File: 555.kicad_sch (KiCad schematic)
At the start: 62 parts, among them J2 Screw_Terminal_01x02, P1 USB_C_Plug, SW1 SW_Push, SW2 SW_Push, SW3 SW_Push, SW4 SW_Push, SW5 SW_Push, SW6 SW_Push, SW7 SW_Push, SW8 SW_Push, U1 NE555P

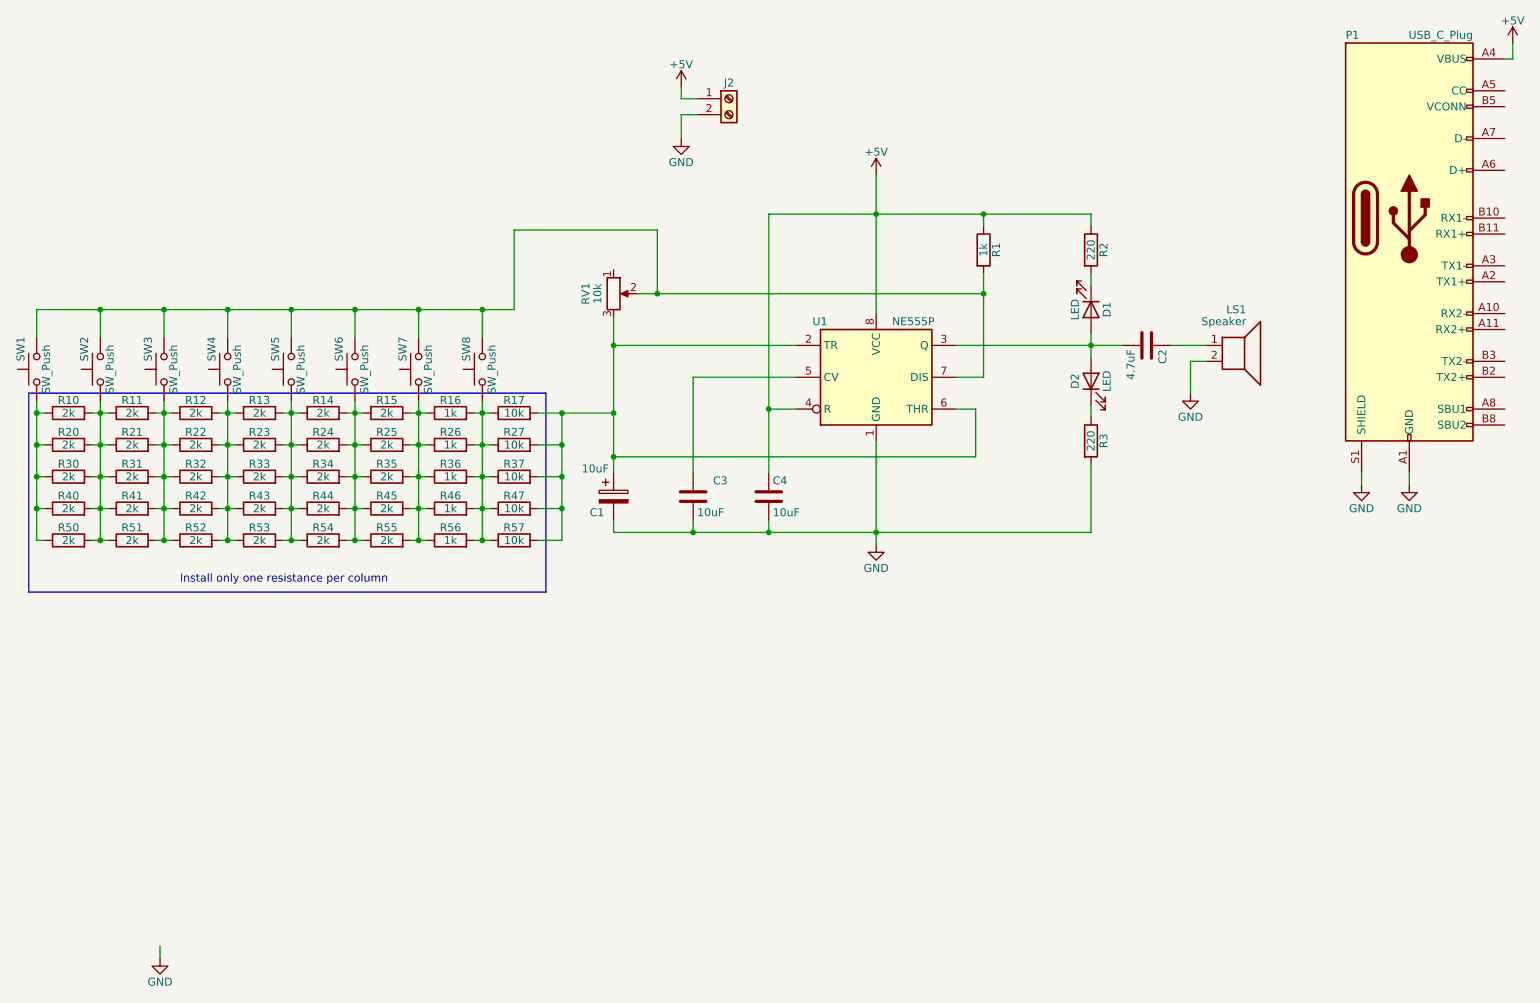
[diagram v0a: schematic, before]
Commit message: Simpler, remove the 10k resistor, move the potentiometer to full to play
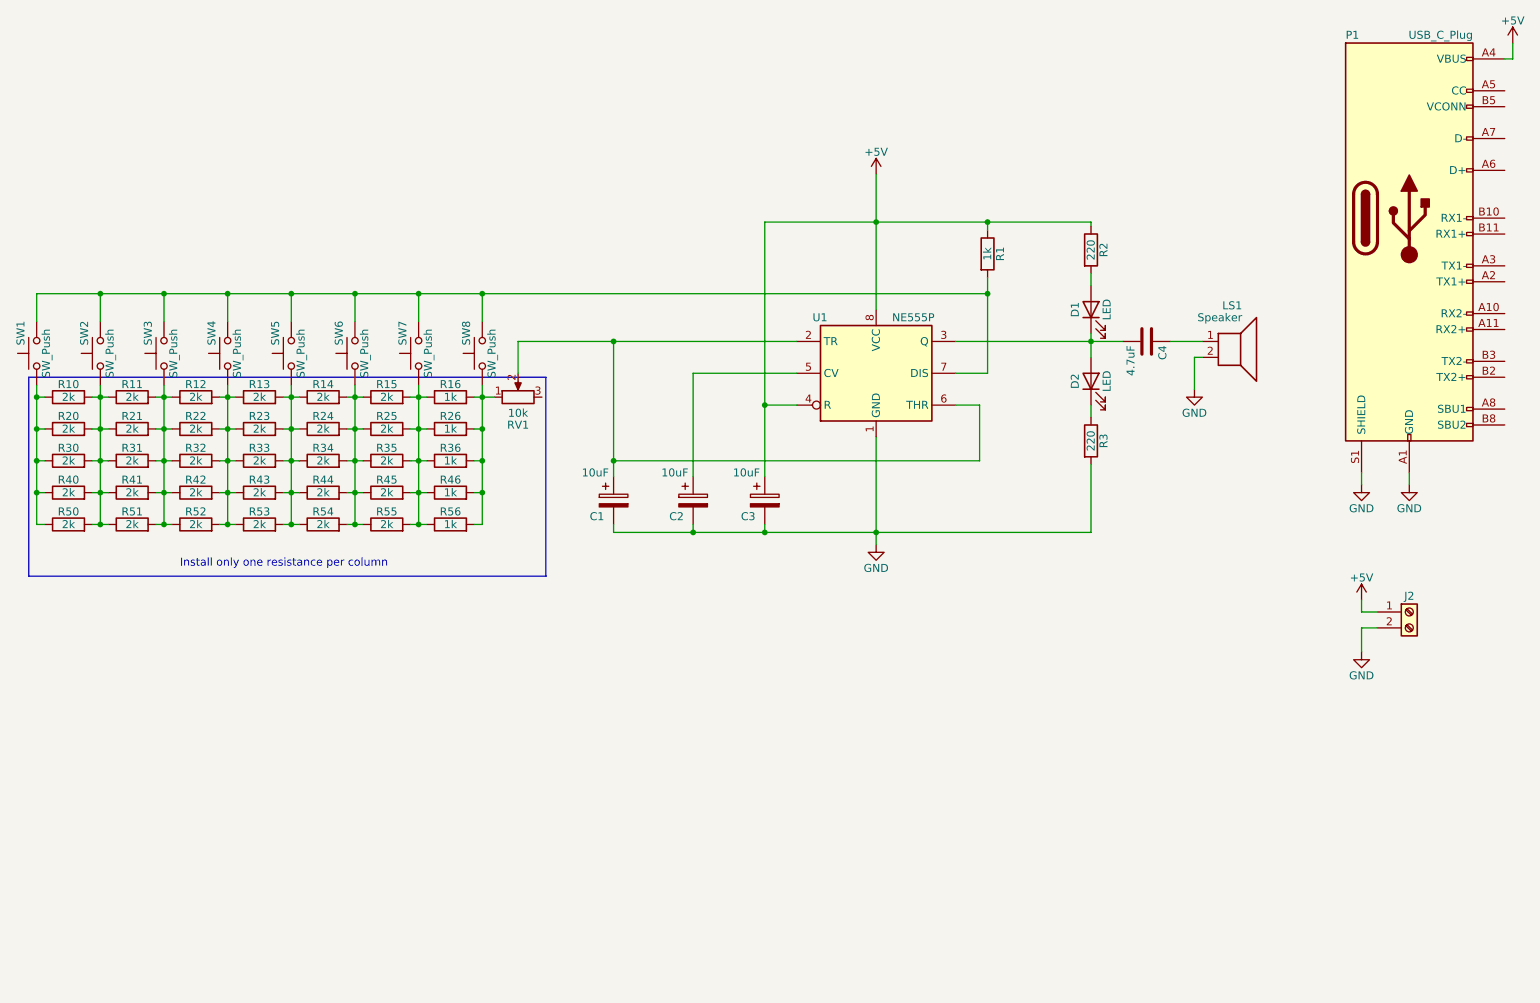
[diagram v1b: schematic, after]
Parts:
- removed C3, C4: 10uF, Capacitor_THT:CP_Radial_D5.0mm_P2.00mm, symbol Device:C
- removed R17: 10k, Resistor_THT:R_Axial_DIN0207_L6.3mm_D2.5mm_P10.16mm_Horizontal, symbol Device:R
- removed R27: 10k, Resistor_SMD:R_1206_3216Metric, symbol Device:R
- removed R37: 10k, Resistor_SMD:R_0603_1608Metric, symbol Device:R
- removed R47: 10k, Resistor_SMD:R_0402_1005Metric, symbol Device:R
- removed R57: 10k, Resistor_SMD:R_0201_0603Metric, symbol Device:R
- added C2, C3: 10uF, Capacitor_THT:CP_Radial_D5.0mm_P2.00mm, symbol Device:C_Polarized
- renumbered C2 to C4
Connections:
- net +5V: now also C3.1
- net GND: now also C2.2, C3.2
- net at R16.2, R26.2, R36.2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: now also RV1.1
- net at C1.1, U1.2 (TR), U1.6 (THR): now also RV1.2; no longer RV1.3
- net at U1.5 (CV): now also C2.1
- net at R2.2: now also D1.2 (A); no longer D1.1 (K)
- net at R1.2, SW1.2, SW2.2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: no longer RV1.2
- net at C4.2, D2.2 (A), U1.3 (Q): now also D1.1 (K); no longer D1.2 (A)
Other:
- moved on the sheet: C1, C4, D1, J2, LS1, R1, R10, R11, R12, R13, R14, R15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

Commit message: PCB updated
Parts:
- removed C4: 4.7uF, Capacitor_THT:CP_Radial_D5.0mm_P2.00mm, symbol Device:C
- added C4: 10uF, Capacitor_THT:CP_Radial_D5.0mm_P2.00mm, symbol Device:C_Polarized
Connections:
- net at D1.1 (K), D2.2 (A), U1.3 (Q): now also C4.1
- net at LS1.1: now also C4.2
- no-connect marks 0 -> 14
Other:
- moved on the sheet: P1
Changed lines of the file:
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@@
   (junction (at 75.565 116.84) (diameter 0) (color 0 0 0 0)
   )
+  (no_connect (at 279.4 99.06))
+  (no_connect (at 279.4 60.96))
+  (no_connect (at 279.4 96.52))
+  (no_connect (at 279.4 55.88))
+  (no_connect (at 279.4 81.28))
+  (no_connect (at 279.4 73.66))
+  (no_connect (at 279.4 66.04))
+  (no_connect (at 279.4 88.9))
+  (no_connect (at 279.4 83.82))
+  (no_connect (at 279.4 106.68))
+  (no_connect (at 279.4 91.44))
+  (no_connect (at 279.4 53.34))
+  (no_connect (at 279.4 104.14))
+  (no_connect (at 279.4 76.2))
   (wire (pts (xy 53.975 111.76) (xy 55.245 111.76))
     (stroke (width 0) (type default) (color 0 0 0 0))
@@
     (stroke (width 0) (type default) (color 0 0 0 0))
   )
-  (wire (pts (xy 264.16 113.665) (xy 264.16 115.57))
+  (wire (pts (xy 264.16 114.3) (xy 264.16 115.57))
     (stroke (width 0) (type default) (color 0 0 0 0))
   )
@@
     (stroke (width 0) (type default) (color 0 0 0 0))
   )
-  (wire (pts (xy 280.67 47.625) (xy 280.67 45.085))
+  (wire (pts (xy 280.67 48.26) (xy 280.67 45.72))
     (stroke (width 0) (type default) (color 0 0 0 0))
   )
@@
     (stroke (width 0) (type default) (color 0 0 0 0))
   )
-  (wire (pts (xy 279.4 47.625) (xy 280.67 47.625))
+  (wire (pts (xy 279.4 48.26) (xy 280.67 48.26))
     (stroke (width 0) (type default) (color 0 0 0 0))
   )
@@
     (stroke (width 0) (type default) (color 0 0 0 0))
   )
-  (wire (pts (xy 256.54 113.665) (xy 256.54 115.57))
+  (wire (pts (xy 256.54 114.3) (xy 256.54 115.57))
     (stroke (width 0) (type default) (color 0 0 0 0))
   )
@@
     (pin "2")
   )
-  (symbol (lib_id "power:+5V") (at 280.67 45.085 0) (unit 1)
-    (in_bom yes) (on_board yes)
-    (property "Reference" "#PWR0108" (id 0) (at 280.67 48.895 0)
-      (effects (font (size 1.27 1.27)) hide)
-    )
-    (property "Value" "+5V" (id 1) (at 280.67 41.529 0))
-    (property "Footprint" "" (id 2) (at 280.67 45.085 0)
-      (effects (font (size 1.27 1.27)) hide)
-    )
-    (property "Datasheet" "" (id 3) (at 280.67 45.085 0)
+  (symbol (lib_id "power:+5V") (at 280.67 45.72 0) (unit 1)
+    (in_bom yes) (on_board yes)
+    (property "Reference" "#PWR0108" (id 0) (at 280.67 49.53 0)
+      (effects (font (size 1.27 1.27)) hide)
+    )
+    (property "Value" "+5V" (id 1) (at 280.67 42.164 0))
+    (property "Footprint" "" (id 2) (at 280.67 45.72 0)
+      (effects (font (size 1.27 1.27)) hide)
+    )
+    (property "Datasheet" "" (id 3) (at 280.67 45.72 0)
       (effects (font (size 1.27 1.27)) hide)
     )
@@
     )
     (property "Vendor" "Digikey" (id 5) (at 111.125 111.76 0)
+      (effects (font (size 1.27 1.27)) hide)
+    )
+    (pin "1")
+    (pin "2")
+  )
+  (symbol (lib_id "Device:C_Polarized") (at 222.25 92.71 90) (unit 1)
+    (in_bom yes) (on_board yes)
+    (property "Reference" "C4" (id 0) (at 224.79 96.52 0)
+      (effects (font (size 1.27 1.27)) (justify left))
+    )
+    (property "Value" "10uF" (id 1) (at 217.805 97.79 0)
+      (effects (font (size 1.27 1.27)) (justify left))
+    )
+    (property "Footprint" "Capacitor_THT:CP_Radial_D5.0mm_P2.00mm" (id 2) (at 226.06 91.7448 0)
+      (effects (font (size 1.27 1.27)) hide)
+    )
+    (property "Datasheet" "~" (id 3) (at 222.25 92.71 0)
+      (effects (font (size 1.27 1.27)) hide)
+    )
+    (property "Manufacturer part number" "732-8625-1-ND" (id 4) (at 222.25 92.71 0)
+      (effects (font (size 1.27 1.27)) hide)
+    )
+    (property "Vendor" "Digikey" (id 5) (at 222.25 92.71 0)
       (effects (font (size 1.27 1.27)) hide)
     )
@@
     (pin "7")
   )
-  (symbol (lib_id "Connector:USB_C_Plug") (at 264.16 73.025 0) (unit 1)
-    (in_bom yes) (on_board yes)
-    (property "Reference" "P1" (id 0) (at 254 43.815 0)
+  (symbol (lib_id "Connector:USB_C_Plug") (at 264.16 73.66 0) (unit 1)
+    (in_bom yes) (on_board yes)
+    (property "Reference" "P1" (id 0) (at 254 44.45 0)
       (effects (font (size 1.27 1.27)) (justify left))
     )
-    (property "Value" "USB_C_Plug" (id 1) (at 274.32 43.815 0)
+    (property "Value" "USB_C_Plug" (id 1) (at 274.32 44.45 0)
       (effects (font (size 1.27 1.27)) (justify right))
     )
-    (property "Footprint" "Connector_USB:USB_C_Receptacle_GCT_USB4085" (id 2) (at 267.97 73.025 0)
-      (effects (font (size 1.27 1.27)) hide)
-    )
-    (property "Datasheet" "https://www.usb.org/sites/default/files/documents/usb_type-c.zip" (id 3) (at 267.97 73.025 0)
-      (effects (font (size 1.27 1.27)) hide)
-    )
-    (property "Manufacturer part number" "2073-USB4085-GF-ACT-ND" (id 4) (at 264.16 73.025 0)
-      (effects (font (size 1.27 1.27)) hide)
-    )
-    (property "Vendor" "Digikey" (id 5) (at 264.16 73.025 0)
+    (property "Footprint" "Connector_USB:USB_C_Receptacle_GCT_USB4085" (id 2) (at 267.97 73.66 0)
+      (effects (font (size 1.27 1.27)) hide)
+    )
+    (property "Datasheet" "https://www.usb.org/sites/default/files/documents/usb_type-c.zip" (id 3) (at 267.97 73.66 0)
+      (effects (font (size 1.27 1.27)) hide)
+    )
+    (property "Manufacturer part number" "2073-USB4085-GF-ACT-ND" (id 4) (at 264.16 73.66 0)
+      (effects (font (size 1.27 1.27)) hide)
+    )
+    (property "Vendor" "Digikey" (id 5) (at 264.16 73.66 0)
       (effects (font (size 1.27 1.27)) hide)
     )
@@
     (pin "2")
   )
-  (symbol (lib_id "Device:C") (at 222.25 92.71 270) (unit 1)
-    (in_bom yes) (on_board yes)
-    (property "Reference" "C4" (id 0) (at 224.79 93.345 0)
-      (effects (font (size 1.27 1.27)) (justify left))
-    )
-    (property "Value" "4.7uF" (id 1) (at 219.71 93.345 0)
-      (effects (font (size 1.27 1.27)) (justify left))
-    )
-    (property "Footprint" "Capacitor_THT:CP_Radial_D5.0mm_P2.00mm" (id 2) (at 218.44 93.6752 0)
-      (effects (font (size 1.27 1.27)) hide)
-    )
-    (property "Datasheet" "~" (id 3) (at 222.25 92.71 0)
-      (effects (font (size 1.27 1.27)) hide)
-    )
-    (property "Manufacturer part number" "732-8624-1-ND" (id 4) (at 222.25 92.71 0)
-      (effects (font (size 1.27 1.27)) hide)
-    )
-    (property "Vendor" "Digikey" (id 5) (at 222.25 92.71 0)
-      (effects (font (size 1.27 1.27)) hide)
-    )
-    (pin "1")
-    (pin "2")
-  )
   (symbol (lib_id "Device:R_Potentiometer") (at 121.92 101.6 90) (unit 1)
     (in_bom yes) (on_board yes)
@@
       (reference "C3") (unit 1) (value "10uF") (footprint "Capacitor_THT:CP_Radial_D5.0mm_P2.00mm")
     )
-    (path "/eb43cd7a-b92d-4126-827e-05ce5f51b08c"
-      (reference "C4") (unit 1) (value "4.7uF") (footprint "Capacitor_THT:CP_Radial_D5.0mm_P2.00mm")
+    (path "/82891a1c-a18b-4efc-9f51-de6998f62d8c"
+      (reference "C4") (unit 1) (value "10uF") (footprint "Capacitor_THT:CP_Radial_D5.0mm_P2.00mm")
     )
     (path "/9f5756e1-f166-4e69-8e27-f4d7349d5b5c"

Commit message: Prettier sch
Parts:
- removed P1: USB_C_Plug, Connector_USB:USB_C_Receptacle_GCT_USB4085, symbol Connector:USB_C_Plug
- added P1: USB_C_Plug_USB2.0, Connector_USB:USB_C_Receptacle_GCT_USB4085, symbol Connector:USB_C_Plug_USB2.0
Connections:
- net +5V: now also P1.A4 (VBUS), P1.A9 (VBUS), P1.B4 (VBUS), P1.B9 (VBUS)
- net GND: now also P1.A1 (GND), P1.A12 (GND), P1.B1 (GND), P1.B12 (GND), P1.S1 (SHIELD)
- no-connect marks 14 -> 4
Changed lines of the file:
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@@
   (junction (at 75.565 116.84) (diameter 0) (color 0 0 0 0)
   )
-  (no_connect (at 279.4 99.06))
   (no_connect (at 279.4 60.96))
-  (no_connect (at 279.4 96.52))
   (no_connect (at 279.4 55.88))
-  (no_connect (at 279.4 81.28))
-  (no_connect (at 279.4 73.66))
   (no_connect (at 279.4 66.04))
-  (no_connect (at 279.4 88.9))
-  (no_connect (at 279.4 83.82))
-  (no_connect (at 279.4 106.68))
-  (no_connect (at 279.4 91.44))
   (no_connect (at 279.4 53.34))
-  (no_connect (at 279.4 104.14))
-  (no_connect (at 279.4 76.2))
   (wire (pts (xy 53.975 111.76) (xy 55.245 111.76))
     (stroke (width 0) (type default) (color 0 0 0 0))
@@
     (stroke (width 0) (type default) (color 0 0 0 0))
   )
-  (wire (pts (xy 264.16 114.3) (xy 264.16 115.57))
+  (wire (pts (xy 264.16 86.36) (xy 264.16 87.63))
     (stroke (width 0) (type default) (color 0 0 0 0))
   )
@@
     (stroke (width 0) (type default) (color 0 0 0 0))
   )
-  (wire (pts (xy 256.54 114.3) (xy 256.54 115.57))
+  (wire (pts (xy 256.54 86.36) (xy 256.54 87.63))
     (stroke (width 0) (type default) (color 0 0 0 0))
   )
@@
     (pin "2")
   )
-  (symbol (lib_id "power:GND") (at 264.16 115.57 0) (unit 1)
-    (in_bom yes) (on_board yes)
-    (property "Reference" "#PWR0107" (id 0) (at 264.16 121.92 0)
-      (effects (font (size 1.27 1.27)) hide)
-    )
-    (property "Value" "GND" (id 1) (at 264.16 119.38 0))
-    (property "Footprint" "" (id 2) (at 264.16 115.57 0)
-      (effects (font (size 1.27 1.27)) hide)
-    )
-    (property "Datasheet" "" (id 3) (at 264.16 115.57 0)
+  (symbol (lib_id "power:GND") (at 264.16 87.63 0) (unit 1)
+    (in_bom yes) (on_board yes)
+    (property "Reference" "#PWR0107" (id 0) (at 264.16 93.98 0)
+      (effects (font (size 1.27 1.27)) hide)
+    )
+    (property "Value" "GND" (id 1) (at 264.16 91.44 0))
+    (property "Footprint" "" (id 2) (at 264.16 87.63 0)
+      (effects (font (size 1.27 1.27)) hide)
+    )
+    (property "Datasheet" "" (id 3) (at 264.16 87.63 0)
       (effects (font (size 1.27 1.27)) hide)
     )
@@
     (pin "2")
   )
+  (symbol (lib_id "Connector:USB_C_Plug_USB2.0") (at 264.16 63.5 0) (unit 1)
+    (in_bom yes) (on_board yes) (fields_autoplaced)
+    (property "Reference" "P1" (id 0) (at 264.16 42.0202 0))
+    (property "Value" "USB_C_Plug_USB2.0" (id 1) (at 264.16 44.5571 0))
+    (property "Footprint" "Connector_USB:USB_C_Receptacle_GCT_USB4085" (id 2) (at 267.97 63.5 0)
+      (effects (font (size 1.27 1.27)) hide)
+    )
+    (property "Datasheet" "https://www.usb.org/sites/default/files/documents/usb_type-c.zip" (id 3) (at 267.97 63.5 0)
+      (effects (font (size 1.27 1.27)) hide)
+    )
+    (pin "A1")
+    (pin "A12")
+    (pin "A4")
+    (pin "A5")
+    (pin "A6")
+    (pin "A7")
+    (pin "A9")
+    (pin "B1")
+    (pin "B12")
+    (pin "B4")
+    (pin "B5")
+    (pin "B9")
+    (pin "S1")
+  )
   (symbol (lib_id "Device:R") (at 213.36 108.585 0) (unit 1)
     (in_bom yes) (on_board yes)
@@
     (pin "2")
   )
-  (symbol (lib_id "power:GND") (at 256.54 115.57 0) (unit 1)
-    (in_bom yes) (on_board yes)
-    (property "Reference" "#PWR0106" (id 0) (at 256.54 121.92 0)
-      (effects (font (size 1.27 1.27)) hide)
-    )
-    (property "Value" "GND" (id 1) (at 256.54 119.38 0))
-    (property "Footprint" "" (id 2) (at 256.54 115.57 0)
-      (effects (font (size 1.27 1.27)) hide)
-    )
-    (property "Datasheet" "" (id 3) (at 256.54 115.57 0)
+  (symbol (lib_id "power:GND") (at 256.54 87.63 0) (unit 1)
+    (in_bom yes) (on_board yes)
+    (property "Reference" "#PWR0106" (id 0) (at 256.54 93.98 0)
+      (effects (font (size 1.27 1.27)) hide)
+    )
+    (property "Value" "GND" (id 1) (at 256.54 91.44 0))
+    (property "Footprint" "" (id 2) (at 256.54 87.63 0)
+      (effects (font (size 1.27 1.27)) hide)
+    )
+    (property "Datasheet" "" (id 3) (at 256.54 87.63 0)
       (effects (font (size 1.27 1.27)) hide)
     )
@@
     (pin "7")
   )
-  (symbol (lib_id "Connector:USB_C_Plug") (at 264.16 73.66 0) (unit 1)
-    (in_bom yes) (on_board yes)
-    (property "Reference" "P1" (id 0) (at 254 44.45 0)
-      (effects (font (size 1.27 1.27)) (justify left))
-    )
-    (property "Value" "USB_C_Plug" (id 1) (at 274.32 44.45 0)
-      (effects (font (size 1.27 1.27)) (justify right))
-    )
-    (property "Footprint" "Connector_USB:USB_C_Receptacle_GCT_USB4085" (id 2) (at 267.97 73.66 0)
-      (effects (font (size 1.27 1.27)) hide)
-    )
-    (property "Datasheet" "https://www.usb.org/sites/default/files/documents/usb_type-c.zip" (id 3) (at 267.97 73.66 0)
-      (effects (font (size 1.27 1.27)) hide)
-    )
-    (property "Manufacturer part number" "2073-USB4085-GF-ACT-ND" (id 4) (at 264.16 73.66 0)
-      (effects (font (size 1.27 1.27)) hide)
-    )
-    (property "Vendor" "Digikey" (id 5) (at 264.16 73.66 0)
-      (effects (font (size 1.27 1.27)) hide)
-    )
-    (pin "A1")
-    (pin "A10")
-    (pin "A11")
-    (pin "A12")
-    (pin "A2")
-    (pin "A3")
-    (pin "A4")
-    (pin "A5")
-    (pin "A6")
-    (pin "A7")
-    (pin "A8")
-    (pin "A9")
-    (pin "B1")
-    (pin "B10")
-    (pin "B11")
-    (pin "B12")
-    (pin "B2")
-    (pin "B3")
-    (pin "B4")
-    (pin "B5")
-    (pin "B8")
-    (pin "B9")
-    (pin "S1")
-  )
   (symbol (lib_id "Device:R") (at 50.165 111.76 90) (unit 1)
     (in_bom yes) (on_board yes)
@@
       (reference "LS1") (unit 1) (value "Speaker") (footprint "TerminalBlock_Phoenix:TerminalBlock_Phoenix_PT-1,5-2-5.0-H_1x02_P5.00mm_Horizontal")
     )
-    (path "/afd2edba-b4b3-48f6-9e77-a078bc432dd3"
-      (reference "P1") (unit 1) (value "USB_C_Plug") (footprint "Connector_USB:USB_C_Receptacle_GCT_USB4085")
+    (path "/078c02b2-38b1-4cd7-b8df-c67e584f40da"
+      (reference "P1") (unit 1) (value "USB_C_Plug_USB2.0") (footprint "Connector_USB:USB_C_Receptacle_GCT_USB4085")
     )
     (path "/656aa297-b08e-46a3-8edc-e1ae84d4ed47"
